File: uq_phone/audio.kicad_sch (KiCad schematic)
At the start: 37 parts, among them J10 Conn_01x02, J9 SJ-3551B-MSMT-TR-67, U10 TS3A5018RSVR, U11 NAU88C22YG

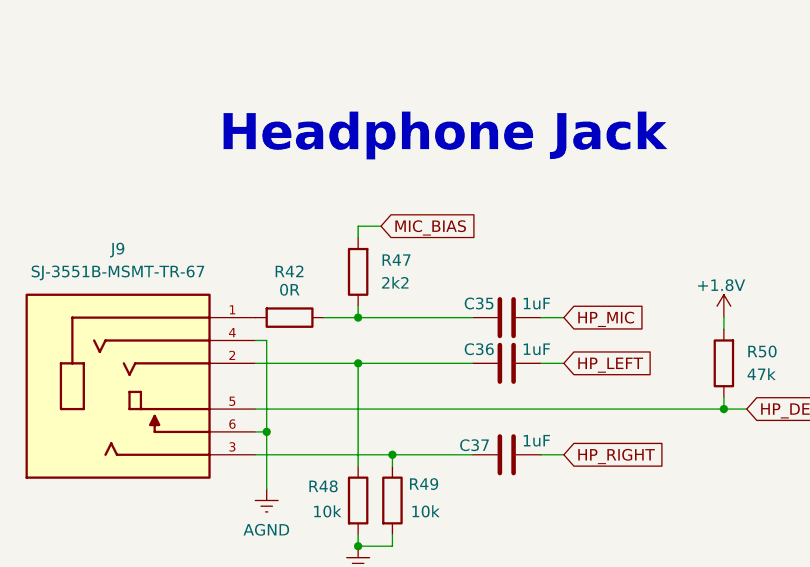
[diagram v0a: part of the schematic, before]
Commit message: Update LCD, Add Programer, Shrink Footprints
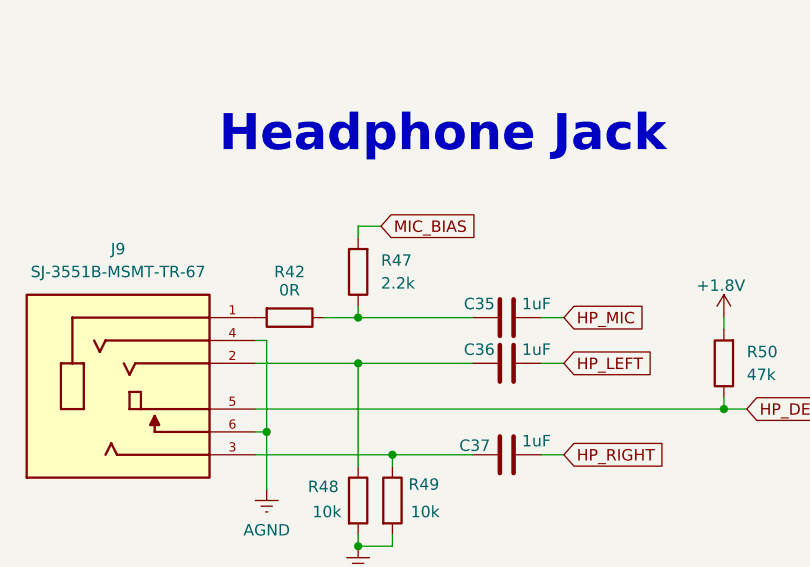
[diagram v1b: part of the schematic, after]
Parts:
- R40, R41, R48, R49, R50: footprint Resistor_SMD:R_0603_1608Metric -> Resistor_SMD:R_0402_1005Metric
- R47: value 2k2 -> 2.2k
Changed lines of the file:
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@@
 			)
 		)
-		(property "Value" "2k2"
+		(property "Value" "2.2k"
 			(at 80.01 236.2199 0)
 			(effects
@@
 			)
 		)
-		(property "Footprint" "Resistor_SMD:R_0603_1608Metric"
+		(property "Footprint" "Resistor_SMD:R_0402_1005Metric"
 			(at 77.47 256.54 0)
 			(effects
@@
 			)
 		)
-		(property "Description" ""
+		(property "Description" "RES SMD 10K OHM 1% 1/10W 0402"
 			(at 77.47 256.54 0)
 			(effects
@@
 			)
 		)
-		(property "Footprint" "Resistor_SMD:R_0603_1608Metric"
+		(property "Footprint" "Resistor_SMD:R_0402_1005Metric"
 			(at 81.28 256.54 0)
 			(effects
@@
 			)
 		)
-		(property "Description" ""
+		(property "Description" "RES SMD 10K OHM 1% 1/10W 0402"
 			(at 81.28 256.54 0)
 			(effects
@@
 			)
 		)
-		(property "Footprint" "Resistor_SMD:R_0603_1608Metric"
+		(property "Footprint" "Resistor_SMD:R_0402_1005Metric"
 			(at 34.29 162.56 0)
 			(effects
@@
 			)
 		)
-		(property "Description" ""
+		(property "Description" "RES SMD 10K OHM 1% 1/10W 0402"
 			(at 34.29 162.56 0)
 			(effects
@@
 			)
 		)
-		(property "Footprint" "Resistor_SMD:R_0603_1608Metric"
+		(property "Footprint" "Resistor_SMD:R_0402_1005Metric"
 			(at 34.29 149.86 0)
 			(effects
@@
 			)
 		)
-		(property "Description" ""
+		(property "Description" "RES SMD 10K OHM 1% 1/10W 0402"
 			(at 34.29 149.86 0)
 			(effects
@@
 			)
 		)
-		(property "Footprint" "Resistor_SMD:R_0603_1608Metric"
+		(property "Footprint" "Resistor_SMD:R_0402_1005Metric"
 			(at 118.11 248.92 0)
 			(effects
@@
 			)
 		)
-		(property "Description" ""
+		(property "Description" "RES SMD 47K OHM 1% 1/10W 0402"
 			(at 118.11 248.92 0)
 			(effects

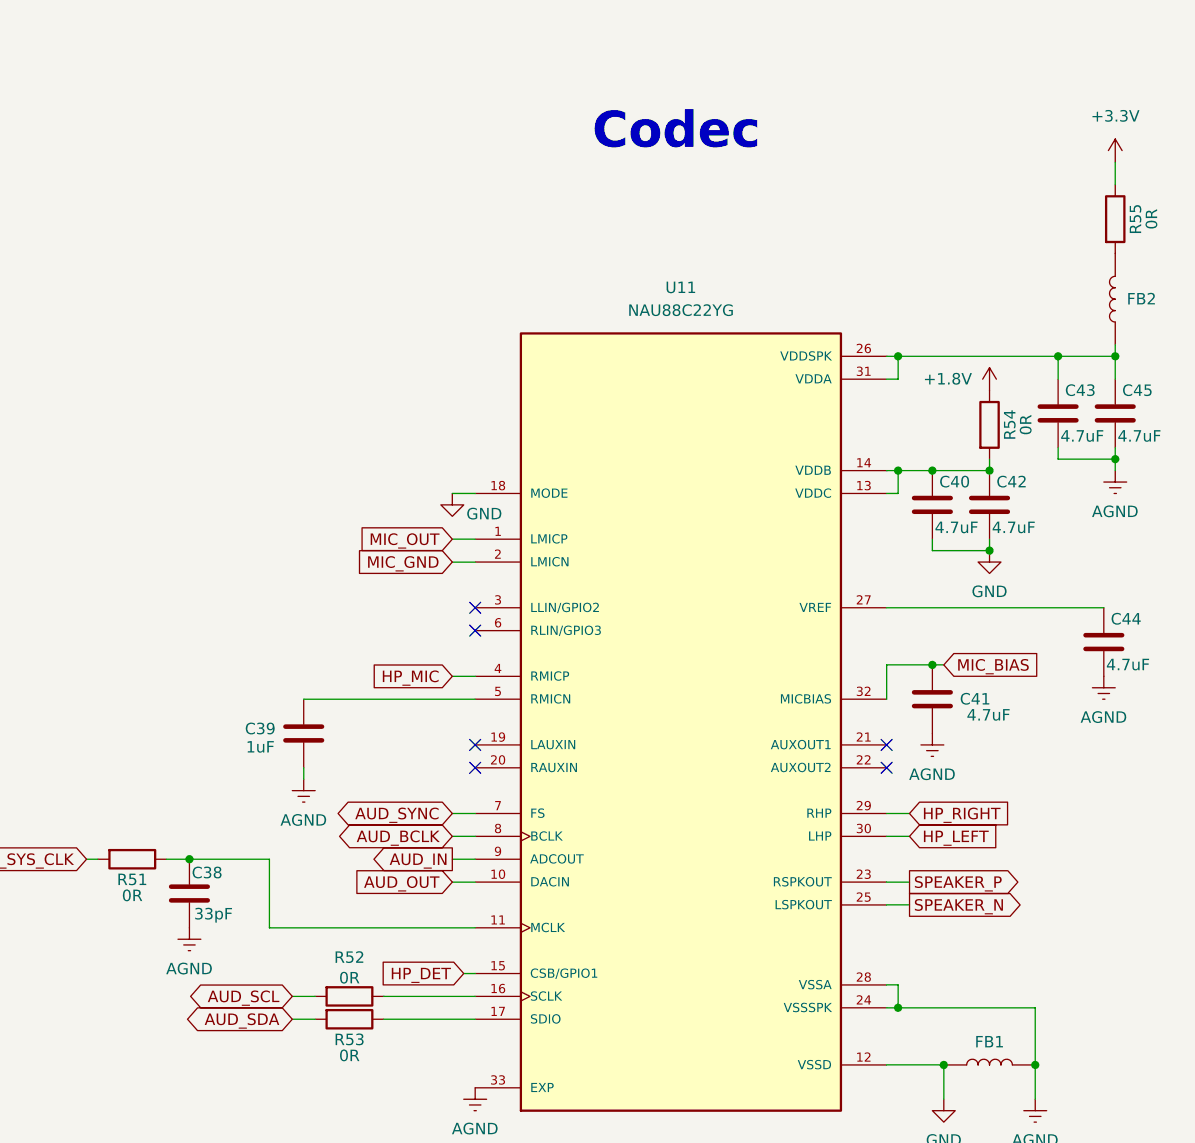
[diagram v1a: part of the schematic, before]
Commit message: Shrink More footprints, rearragment of PCB
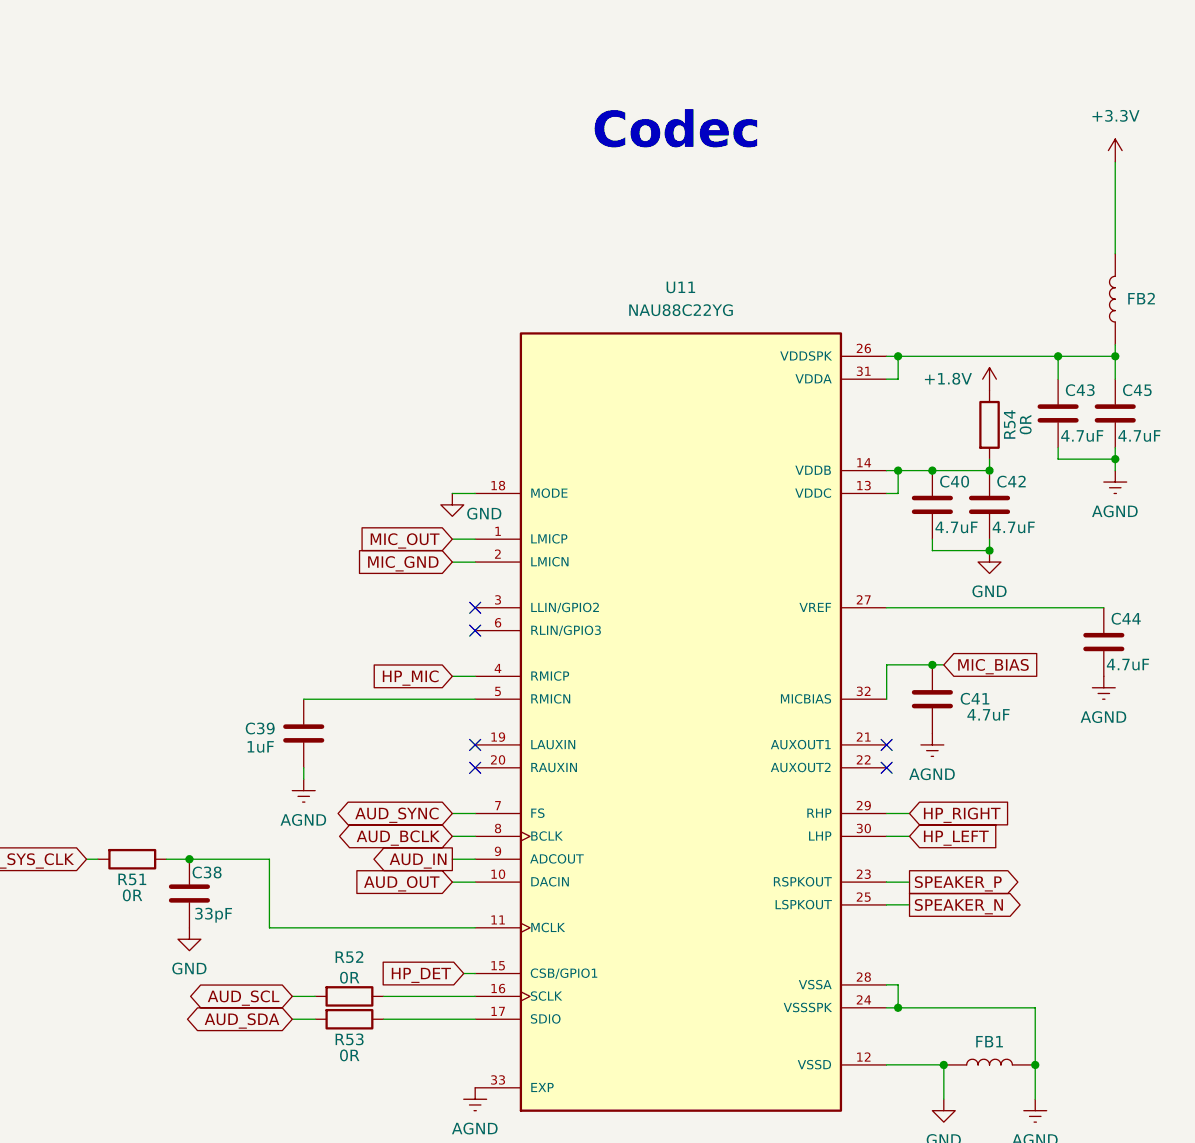
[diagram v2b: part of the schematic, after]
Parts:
- removed R55: 0R, Resistor_SMD:R_0603_1608Metric, symbol Resistors:Resistor_0R
- C34, C35, C36, C37, C38, C39, C40, C41, C42, C43, C44, C45, C46, C47: footprint Capacitor_SMD:C_0603_1608Metric -> Capacitor_SMD:C_0402_1005Metric
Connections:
- net +3.3V: now also FB2.2
- net AGND: no longer C38.2
- net GND: now also C38.2
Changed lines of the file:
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@@
 	(wire
 		(pts
-			(xy 316.23 118.11) (xy 316.23 120.65)
+			(xy 316.23 118.11) (xy 316.23 128.27)
 		)
 		(stroke
@@
 			)
 		)
-		(property "Footprint" "Capacitor_SMD:C_0603_1608Metric"
+		(property "Footprint" "Capacitor_SMD:C_0402_1005Metric"
 			(at 309.88 146.05 0)
 			(effects
@@
 			)
 		)
-		(property "Description" ""
+		(property "Description" "4.7 µF ±10% 6.3V Ceramic Capacitor X5R 0402 (1005 Metric)"
 			(at 309.88 146.05 0)
 			(effects
@@
 	)
 	(symbol
-		(lib_id "power:GNDREF")
-		(at 213.36 203.2 0)
-		(unit 1)
-		(exclude_from_sim no)
-		(in_bom yes)
-		(on_board yes)
-		(dnp no)
-		(property "Reference" "#PWR097"
-			(at 213.36 209.55 0)
-			(effects
-				(font
-					(size 1.27 1.27)
-				)
-				(hide yes)
-			)
-		)
-		(property "Value" "AGND"
-			(at 213.36 207.772 0)
-			(effects
-				(font
-					(size 1.27 1.27)
-				)
-			)
-		)
-		(property "Footprint" ""
-			(at 213.36 203.2 0)
-			(effects
-				(font
-					(size 1.27 1.27)
-				)
-				(hide yes)
-			)
-		)
-		(property "Datasheet" ""
-			(at 213.36 203.2 0)
-			(effects
-				(font
-					(size 1.27 1.27)
-				)
-				(hide yes)
-			)
-		)
-		(property "Description" "Power symbol creates a global label with name \"GNDREF\" , reference supply ground"
-			(at 213.36 203.2 0)
-			(effects
-				(font
-					(size 1.27 1.27)
-				)
-				(hide yes)
-			)
-		)
-		(pin "1"
-		)
-		(instances
-			(project "uq_phone"
-				(path "/14f57415-6807-40a5-bb38-3cb818a2cdae/e19f4f8c-44cb-4a36-b4d3-60ff6ff42a2f"
-					(reference "#PWR097")
-					(unit 1)
-				)
-			)
-		)
-	)
-	(symbol
 		(lib_id "power:+1V8")
 		(at 49.53 127 0)
@@
 	)
 	(symbol
-		(lib_id "Resistors:Resistor_0R")
-		(at 316.23 124.46 180)
-		(unit 1)
-		(exclude_from_sim no)
-		(in_bom yes)
-		(on_board yes)
-		(dnp no)
-		(property "Reference" "R55"
-			(at 318.516 124.46 90)
-			(effects
-				(font
-					(size 1.27 1.27)
-				)
-			)
-		)
-		(property "Value" "0R"
-			(at 320.294 124.46 90)
-			(effects
-				(font
-					(size 1.27 1.27)
-				)
-			)
-		)
-		(property "Footprint" "Resistor_SMD:R_0603_1608Metric"
-			(at 316.23 120.65 0)
-			(effects
-				(font
-					(size 1.27 1.27)
-				)
-				(hide yes)
-			)
-		)
-		(property "Datasheet" ""
-			(at 316.23 120.65 0)
-			(effects
-				(font
-					(size 1.27 1.27)
-				)
-				(hide yes)
-			)
-		)
-		(property "Description" ""
-			(at 316.23 120.65 0)
-			(effects
-				(font
-					(size 1.27 1.27)
-				)
-				(hide yes)
-			)
-		)
-		(pin "2"
-		)
-		(pin "1"
-		)
-		(instances
-			(project "uq_phone"
-				(path "/14f57415-6807-40a5-bb38-3cb818a2cdae/e19f4f8c-44cb-4a36-b4d3-60ff6ff42a2f"
-					(reference "R55")
-					(unit 1)
-				)
-			)
-		)
-	)
-	(symbol
 		(lib_id "power:GNDREF")
 		(at 77.47 265.43 0)
@@
 			)
 		)
-		(property "Footprint" "Capacitor_SMD:C_0603_1608Metric"
+		(property "Footprint" "Capacitor_SMD:C_0402_1005Metric"
 			(at 226.06 181.61 0)
 			(effects
@@
 			)
 		)
-		(property "Description" ""
+		(property "Description" "1 µF ±10% 25V Ceramic Capacitor X5R 0402 (1005 Metric)"
 			(at 226.06 181.61 0)
 			(effects
@@
 			)
 		)
-		(property "Footprint" "Capacitor_SMD:C_0603_1608Metric"
+		(property "Footprint" "Capacitor_SMD:C_0402_1005Metric"
 			(at 274.32 59.69 0)
 			(effects
@@
 			)
 		)
-		(property "Description" ""
+		(property "Description" "1 µF ±10% 25V Ceramic Capacitor X5R 0402 (1005 Metric)"
 			(at 274.32 59.69 0)
 			(effects
@@
 			)
 		)
-		(property "Footprint" "Capacitor_SMD:C_0603_1608Metric"
+		(property "Footprint" "Capacitor_SMD:C_0402_1005Metric"
 			(at 267.97 48.26 0)
 			(effects
@@
 			)
 		)
-		(property "Description" ""
+		(property "Description" "4.7 µF ±10% 6.3V Ceramic Capacitor X5R 0402 (1005 Metric)"
 			(at 267.97 48.26 0)
 			(effects
@@
 			)
 		)
-		(property "Footprint" "Capacitor_SMD:C_0603_1608Metric"
+		(property "Footprint" "Capacitor_SMD:C_0402_1005Metric"
 			(at 213.36 199.39 0)
 			(effects
@@
 			)
 		)
-		(property "Description" ""
+		(property "Description" "CAP CER 33PF 16V X7R 0402"
 			(at 213.36 199.39 0)
 			(effects
@@
 			)
 		)
-		(property "Footprint" "Capacitor_SMD:C_0603_1608Metric"
+		(property "Footprint" "Capacitor_SMD:C_0402_1005Metric"
 			(at 295.91 156.21 0)
 			(effects
@@
 			)
 		)
-		(property "Description" ""
+		(property "Description" "4.7 µF ±10% 6.3V Ceramic Capacitor X5R 0402 (1005 Metric)"
 			(at 295.91 156.21 0)
 			(effects
@@
 			)
 		)
-		(property "Footprint" "Capacitor_SMD:C_0603_1608Metric"
+		(property "Footprint" "Capacitor_SMD:C_0402_1005Metric"
 			(at 295.91 177.8 0)
 			(effects
@@
 			)
 		)
-		(property "Description" ""
+		(property "Description" "4.7 µF ±10% 6.3V Ceramic Capacitor X5R 0402 (1005 Metric)"
 			(at 295.91 177.8 0)
 			(effects
@@
 			)
 		)
-		(property "Footprint" "Capacitor_SMD:C_0603_1608Metric"
+		(property "Footprint" "Capacitor_SMD:C_0402_1005Metric"
 			(at 49.53 133.35 0)
 			(effects
@@
 			)
 		)
-		(property "Description" ""
+		(property "Description" "0.1 µF ±10% 10V Ceramic Capacitor X7R 0402 (1005 Metric)"
 			(at 49.53 133.35 0)
 			(effects
@@
 			)
 		)
-		(property "Footprint" "Capacitor_SMD:C_0603_1608Metric"
+		(property "Footprint" "Capacitor_SMD:C_0402_1005Metric"
 			(at 93.98 255.27 0)
 			(effects
@@
 			)
 		)
-		(property "Description" ""
+		(property "Description" "1 µF ±10% 25V Ceramic Capacitor X5R 0402 (1005 Metric)"
 			(at 93.98 255.27 0)
 			(effects
@@
 	)
 	(symbol
+		(lib_id "power:GND")
+		(at 213.36 203.2 0)
+		(unit 1)
+		(exclude_from_sim no)
+		(in_bom yes)
+		(on_board yes)
+		(dnp no)
+		(property "Reference" "#PWR087"
+			(at 213.36 209.55 0)
+			(effects
+				(font
+					(size 1.27 1.27)
+				)
+				(hide yes)
+			)
+		)
+		(property "Value" "GND"
+			(at 213.36 207.772 0)
+			(effects
+				(font
+					(size 1.27 1.27)
+				)
+			)
+		)
+		(property "Footprint" ""
+			(at 213.36 203.2 0)
+			(effects
+				(font
+					(size 1.27 1.27)
+				)
+				(hide yes)
+			)
+		)
+		(property "Datasheet" ""
+			(at 213.36 203.2 0)
+			(effects
+				(font
+					(size 1.27 1.27)
+				)
+				(hide yes)
+			)
+		)
+		(property "Description" "Power symbol creates a global label with name \"GND\" , ground"
+			(at 213.36 203.2 0)
+			(effects
+				(font
+					(size 1.27 1.27)
+				)
+				(hide yes)
+			)
+		)
+		(pin "1"
+		)
+		(instances
+			(project "uq_phone"
+				(path "/14f57415-6807-40a5-bb38-3cb818a2cdae/e19f4f8c-44cb-4a36-b4d3-60ff6ff42a2f"
+					(reference "#PWR087")
+					(unit 1)
+				)
+			)
+		)
+	)
+	(symbol
 		(lib_id "Resistors:Resistor_10k")
 		(at 34.29 158.75 0)
@@
 			)
 		)
-		(property "Footprint" "Capacitor_SMD:C_0603_1608Metric"
+		(property "Footprint" "Capacitor_SMD:C_0402_1005Metric"
 			(at 314.96 171.45 0)
 			(effects
@@
 			)
 		)
-		(property "Description" ""
+		(property "Description" "4.7 µF ±10% 6.3V Ceramic Capacitor X5R 0402 (1005 Metric)"
 			(at 314.96 171.45 0)
 			(effects
@@
 			)
 		)
-		(property "Footprint" "Capacitor_SMD:C_0603_1608Metric"
+		(property "Footprint" "Capacitor_SMD:C_0402_1005Metric"
 			(at 93.98 245.11 0)
 			(effects
@@
 			)
 		)
-		(property "Description" ""
+		(property "Description" "1 µF ±10% 25V Ceramic Capacitor X5R 0402 (1005 Metric)"
 			(at 93.98 245.11 0)
 			(effects
@@
 			)
 		)
-		(property "Footprint" "Capacitor_SMD:C_0603_1608Metric"
+		(property "Footprint" "Capacitor_SMD:C_0402_1005Metric"
 			(at 93.98 240.03 0)
 			(effects
@@
 			)
 		)
-		(property "Description" ""
+		(property "Description" "1 µF ±10% 25V Ceramic Capacitor X5R 0402 (1005 Metric)"
 			(at 93.98 240.03 0)
 			(effects
@@
 			)
 		)
-		(property "Footprint" "Capacitor_SMD:C_0603_1608Metric"
+		(property "Footprint" "Capacitor_SMD:C_0402_1005Metric"
 			(at 316.23 146.05 0)
 			(effects
@@
 			)
 		)
-		(property "Description" ""
+		(property "Description" "4.7 µF ±10% 6.3V Ceramic Capacitor X5R 0402 (1005 Metric)"
 			(at 316.23 146.05 0)
 			(effects
@@
 			)
 		)
-		(property "Footprint" "Capacitor_SMD:C_0603_1608Metric"
+		(property "Footprint" "Capacitor_SMD:C_0402_1005Metric"
 			(at 302.26 156.21 0)
 			(effects
@@
 			)
 		)
-		(property "Description" ""
+		(property "Description" "4.7 µF ±10% 6.3V Ceramic Capacitor X5R 0402 (1005 Metric)"
 			(at 302.26 156.21 0)
 			(effects

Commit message: Update PCB, minor changes
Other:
- moved on the sheet: C34, J10, R40, R41, R43, R44, R45, R46, U10

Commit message: Changed SIM/uSD port & adjust routing
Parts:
- J10: footprint Connector_Wire:SolderWire-0.5sqmm_1x02_P4.6mm_D0.9mm_OD2.1mm -> Connector_Wire:SolderWire-0.25sqmm_1x02_P4.2mm_D0.65mm_OD1.7mm
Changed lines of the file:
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@@
 			)
 		)
-		(property "Footprint" "Connector_Wire:SolderWire-0.5sqmm_1x02_P4.6mm_D0.9mm_OD2.1mm"
+		(property "Footprint" "Connector_Wire:SolderWire-0.25sqmm_1x02_P4.2mm_D0.65mm_OD1.7mm"
 			(at 87.63 46.99 0)
 			(effects

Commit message: Arrange PCB
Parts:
- removed R52, R53: 0R, Resistor_SMD:R_0603_1608Metric, symbol Resistors:Resistor_0R
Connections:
- net AUD_SCL: now also U11.16 (SCLK)
- net AUD_SDA: now also U11.17 (SDIO)
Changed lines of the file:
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@@
 	(wire
 		(pts
-			(xy 224.79 210.82) (xy 227.33 210.82)
+			(xy 224.79 210.82) (xy 245.11 210.82)
 		)
 		(stroke
@@
 	(wire
 		(pts
-			(xy 234.95 210.82) (xy 245.11 210.82)
-		)
-		(stroke
-			(width 0)
-			(type default)
-		)
-	)
-	(wire
-		(pts
 			(xy 316.23 118.11) (xy 316.23 128.27)
 		)
@@
 	(wire
 		(pts
-			(xy 234.95 213.36) (xy 245.11 213.36)
-		)
-		(stroke
-			(width 0)
-			(type default)
-		)
-	)
-	(wire
-		(pts
 			(xy 58.42 151.13) (xy 62.23 151.13)
 		)
@@
 	(wire
 		(pts
-			(xy 224.79 213.36) (xy 227.33 213.36)
+			(xy 224.79 213.36) (xy 245.11 213.36)
 		)
 		(stroke
@@
 	)
 	(symbol
-		(lib_id "Resistors:Resistor_0R")
-		(at 231.14 213.36 90)
-		(unit 1)
-		(exclude_from_sim no)
-		(in_bom yes)
-		(on_board yes)
-		(dnp no)
-		(property "Reference" "R53"
-			(at 231.14 215.646 90)
-			(effects
-				(font
-					(size 1.27 1.27)
-				)
-			)
-		)
-		(property "Value" "0R"
-			(at 231.14 217.424 90)
-			(effects
-				(font
-					(size 1.27 1.27)
-				)
-			)
-		)
-		(property "Footprint" "Resistor_SMD:R_0603_1608Metric"
-			(at 234.95 213.36 0)
-			(effects
-				(font
-					(size 1.27 1.27)
-				)
-				(hide yes)
-			)
-		)
-		(property "Datasheet" ""
-			(at 234.95 213.36 0)
-			(effects
-				(font
-					(size 1.27 1.27)
-				)
-				(hide yes)
-			)
-		)
-		(property "Description" ""
-			(at 234.95 213.36 0)
-			(effects
-				(font
-					(size 1.27 1.27)
-				)
-				(hide yes)
-			)
-		)
-		(pin "2"
-		)
-		(pin "1"
-		)
-		(instances
-			(project "uq_phone"
-				(path "/14f57415-6807-40a5-bb38-3cb818a2cdae/e19f4f8c-44cb-4a36-b4d3-60ff6ff42a2f"
-					(reference "R53")
-					(unit 1)
-				)
-			)
-		)
-	)
-	(symbol
 		(lib_id "SJ-3551B-MSMT-TR-67:SJ-3551B-MSMT-TR-67")
 		(at 50.8 247.65 0)
@@
 					(unit 1)
 				)
-			)
-		)
-	)
-	(symbol
-		(lib_id "Resistors:Resistor_0R")
-		(at 231.14 210.82 90)
-		(unit 1)
-		(exclude_from_sim no)
-		(in_bom yes)
-		(on_board yes)
-		(dnp no)
-		(property "Reference" "R52"
-			(at 231.14 206.502 90)
-			(effects
-				(font
-					(size 1.27 1.27)
-				)
-			)
-		)
-		(property "Value" "0R"
-			(at 231.14 208.788 90)
-			(effects
-				(font
-					(size 1.27 1.27)
-				)
-			)
-		)
-		(property "Footprint" "Resistor_SMD:R_0603_1608Metric"
-			(at 234.95 210.82 0)
-			(effects
-				(font
-					(size 1.27 1.27)
-				)
-				(hide yes)
-			)
-		)
-		(property "Datasheet" ""
-			(at 234.95 210.82 0)
-			(effects
-				(font
-					(size 1.27 1.27)
-				)
-				(hide yes)
-			)
-		)
-		(property "Description" ""
-			(at 234.95 210.82 0)
-			(effects
-				(font
-					(size 1.27 1.27)
-				)
-				(hide yes)
-			)
-		)
-		(pin "2"
-		)
-		(pin "1"
-		)
-		(instances
-			(project "uq_phone"
-				(path "/14f57415-6807-40a5-bb38-3cb818a2cdae/e19f4f8c-44cb-4a36-b4d3-60ff6ff42a2f"
-					(reference "R52")
-					(unit 1)
-				)
